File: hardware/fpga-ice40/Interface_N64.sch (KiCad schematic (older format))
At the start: 7 parts, among them J4 Conn_02x20_Odd_Even

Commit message: Reannotate schematic symbols
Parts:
- renumbered J4 to J6, RN7 to RN5, RN5 to RN6, RN8 to RN7, RN6 to RN8
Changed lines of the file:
@@
 P 3500 4300
 AR Path="/5F1CD119" Ref="J?"  Part="1"
-AR Path="/5F133F50/5F1CD119" Ref="J4"  Part="1"
-F 0 "J4" H 3550 5350 50  0000 C CNN
+AR Path="/5F133F50/5F1CD119" Ref="J6"  Part="1"
+F 0 "J6" H 3550 5350 50  0000 C CNN
 F 1 "Conn_02x20_Odd_Even" H 3550 5325 50  0001 C CNN
 F 2 "local_conn:PinHeader_2x20_P2.54mm_Horizontal" H 3500 4300 50  0001 C CNN
@@
 N64_OS_EVENTn
 $Comp
-L ng_power:GND #PWR0126
+L ng_power:GND #PWR026
 U 1 1 5F1CD13A
 P 3900 5400
-F 0 "#PWR0126" H 3900 5150 50  0001 C CNN
+F 0 "#PWR026" H 3900 5150 50  0001 C CNN
 F 1 "GND" H 3903 5274 50  0000 C CNN
 F 2 "" H 3800 5050 50  0001 C CNN
@@
 P 5900 4400
 AR Path="/5F1CD15B" Ref="RN?"  Part="1"
-AR Path="/5F133F50/5F1CD15B" Ref="RN5"  Part="1"
-F 0 "RN5" V 5483 4400 50  0000 C CNN
+AR Path="/5F133F50/5F1CD15B" Ref="RN6"  Part="1"
+F 0 "RN6" V 5483 4400 50  0000 C CNN
 F 1 "33R" V 5574 4400 50  0000 C CNN
 F 2 "Resistor_SMD:R_Array_Convex_4x0603" V 6175 4400 50  0001 C CNN
@@
 P 5900 5100
 AR Path="/5F1CD161" Ref="RN?"  Part="1"
-AR Path="/5F133F50/5F1CD161" Ref="RN6"  Part="1"
-F 0 "RN6" V 5483 5100 50  0000 C CNN
+AR Path="/5F133F50/5F1CD161" Ref="RN8"  Part="1"
+F 0 "RN8" V 5483 5100 50  0000 C CNN
 F 1 "33R" V 5574 5100 50  0000 C CNN
 F 2 "Resistor_SMD:R_Array_Convex_4x0603" V 6175 5100 50  0001 C CNN
@@
 P 7750 3700
 AR Path="/5F1CD167" Ref="RN?"  Part="1"
-AR Path="/5F133F50/5F1CD167" Ref="RN7"  Part="1"
-F 0 "RN7" V 7333 3700 50  0000 C CNN
+AR Path="/5F133F50/5F1CD167" Ref="RN5"  Part="1"
+F 0 "RN5" V 7333 3700 50  0000 C CNN
 F 1 "33R" V 7424 3700 50  0000 C CNN
 F 2 "Resistor_SMD:R_Array_Convex_4x0603" V 8025 3700 50  0001 C CNN
@@
 P 7750 4400
 AR Path="/5F1CD16D" Ref="RN?"  Part="1"
-AR Path="/5F133F50/5F1CD16D" Ref="RN8"  Part="1"
-F 0 "RN8" V 7333 4400 50  0000 C CNN
+AR Path="/5F133F50/5F1CD16D" Ref="RN7"  Part="1"
+F 0 "RN7" V 7333 4400 50  0000 C CNN
 F 1 "33R" V 7424 4400 50  0000 C CNN
 F 2 "Resistor_SMD:R_Array_Convex_4x0603" V 8025 4400 50  0001 C CNN

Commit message: Component selection by MPN and routing cleanup
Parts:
- J6: MPN (none) -> C124369
- RN4, RN5, RN6, RN7, RN8, RN9: value 33R -> 33R, 1%; MPN (none) -> YC164-FR-0733RL
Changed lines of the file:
@@
 F 2 "local_conn:PinHeader_2x20_P2.54mm_Horizontal" H 3500 4300 50  0001 C CNN
 F 3 "~" H 3500 4300 50  0001 C CNN
+F 4 "C124369" H 3500 4300 50  0001 C CNN "MPN"
 	1    3500 4300
 	1    0    0    -1
@@
 AR Path="/5F133F50/5F1CD155" Ref="RN4"  Part="1"
 F 0 "RN4" V 5483 3700 50  0000 C CNN
-F 1 "33R" V 5574 3700 50  0000 C CNN
+F 1 "33R, 1%" V 5574 3700 50  0000 C CNN
 F 2 "Resistor_SMD:R_Array_Convex_4x0603" V 6175 3700 50  0001 C CNN
 F 3 "~" H 5900 3700 50  0001 C CNN
+F 4 "YC164-FR-0733RL" H 5900 3700 50  0001 C CNN "MPN"
 	1    5900 3700
 	0    1    1    0
@@
 AR Path="/5F133F50/5F1CD15B" Ref="RN6"  Part="1"
 F 0 "RN6" V 5483 4400 50  0000 C CNN
-F 1 "33R" V 5574 4400 50  0000 C CNN
+F 1 "33R, 1%" V 5574 4400 50  0000 C CNN
 F 2 "Resistor_SMD:R_Array_Convex_4x0603" V 6175 4400 50  0001 C CNN
 F 3 "~" H 5900 4400 50  0001 C CNN
+F 4 "YC164-FR-0733RL" H 5900 4400 50  0001 C CNN "MPN"
 	1    5900 4400
 	0    1    1    0
@@
 AR Path="/5F133F50/5F1CD161" Ref="RN8"  Part="1"
 F 0 "RN8" V 5483 5100 50  0000 C CNN
-F 1 "33R" V 5574 5100 50  0000 C CNN
+F 1 "33R, 1%" V 5574 5100 50  0000 C CNN
 F 2 "Resistor_SMD:R_Array_Convex_4x0603" V 6175 5100 50  0001 C CNN
 F 3 "~" H 5900 5100 50  0001 C CNN
+F 4 "YC164-FR-0733RL" H 5900 5100 50  0001 C CNN "MPN"
 	1    5900 5100
 	0    1    1    0
@@
 AR Path="/5F133F50/5F1CD167" Ref="RN5"  Part="1"
 F 0 "RN5" V 7333 3700 50  0000 C CNN
-F 1 "33R" V 7424 3700 50  0000 C CNN
+F 1 "33R, 1%" V 7424 3700 50  0000 C CNN
 F 2 "Resistor_SMD:R_Array_Convex_4x0603" V 8025 3700 50  0001 C CNN
 F 3 "~" H 7750 3700 50  0001 C CNN
+F 4 "YC164-FR-0733RL" H 7750 3700 50  0001 C CNN "MPN"
 	1    7750 3700
 	0    1    1    0
@@
 AR Path="/5F133F50/5F1CD16D" Ref="RN7"  Part="1"
 F 0 "RN7" V 7333 4400 50  0000 C CNN
-F 1 "33R" V 7424 4400 50  0000 C CNN
+F 1 "33R, 1%" V 7424 4400 50  0000 C CNN
 F 2 "Resistor_SMD:R_Array_Convex_4x0603" V 8025 4400 50  0001 C CNN
 F 3 "~" H 7750 4400 50  0001 C CNN
+F 4 "YC164-FR-0733RL" H 7750 4400 50  0001 C CNN "MPN"
 	1    7750 4400
 	0    1    1    0
@@
 AR Path="/5F133F50/5F1CD183" Ref="RN9"  Part="1"
 F 0 "RN9" V 7333 5100 50  0000 C CNN
-F 1 "33R" V 7424 5100 50  0000 C CNN
+F 1 "33R, 1%" V 7424 5100 50  0000 C CNN
 F 2 "Resistor_SMD:R_Array_Convex_4x0603" V 8025 5100 50  0001 C CNN
 F 3 "~" H 7750 5100 50  0001 C CNN
+F 4 "YC164-FR-0733RL" H 7750 5100 50  0001 C CNN "MPN"
 	1    7750 5100
 	0    1    1    0

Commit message: Completed verification of all pins for all symbols
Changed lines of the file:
@@
 	3200 4100 3200 4000
 Wire Wire Line
-	3200 4000 3100 4000
-Connection ~ 3200 4000
+	3200 3900 3100 3900
 NoConn ~ 3300 3400
 NoConn ~ 3300 3500
@@
 Text GLabel 4000 5300 2    50   Input ~ 0
 N64_AD15
-Text GLabel 3100 4000 0    50   UnSpc ~ 0
+Text GLabel 3100 3900 0    50   UnSpc ~ 0
 N64_3V3
 $Comp
@@
 Text GLabel 7950 4500 2    50   Input ~ 0
 N64_AD7_IC
+Wire Wire Line
+	3200 3900 3200 4000
+Connection ~ 3200 4000
 $EndSCHEMATC

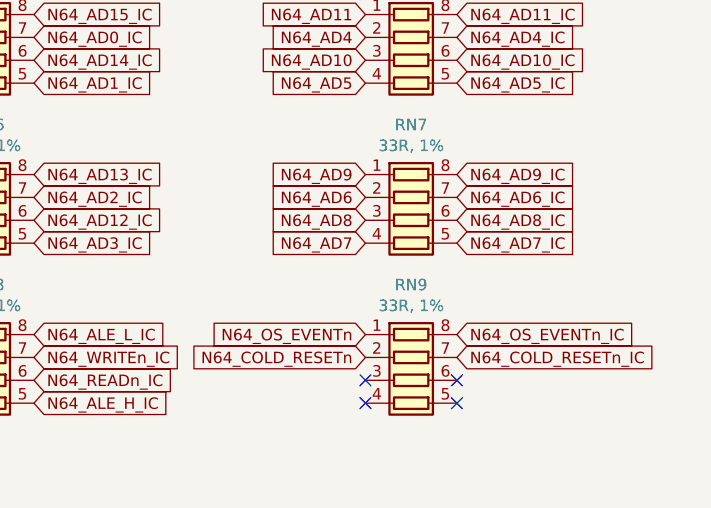
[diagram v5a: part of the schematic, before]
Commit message: Fix mechanical issue by moving USB connector to top of board
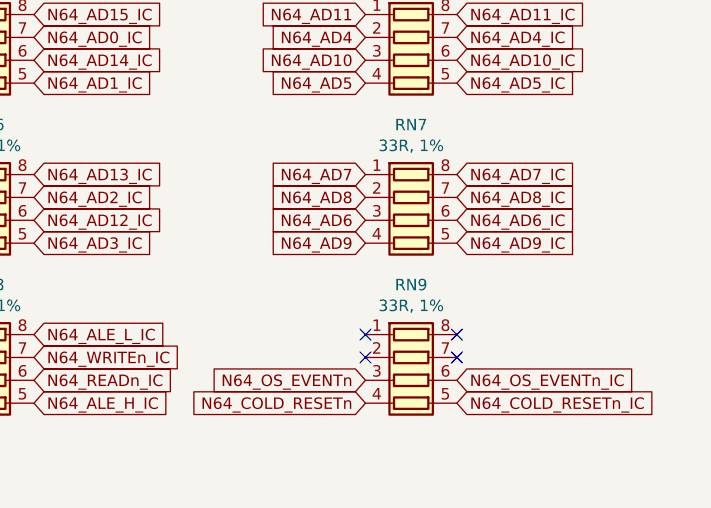
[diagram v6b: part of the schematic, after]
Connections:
- net N64_AD6: now also RN7.3 (R3.1); no longer RN7.2 (R2.1)
- net N64_AD6_IC: now also RN7.6 (R3.2); no longer RN7.7 (R2.2)
- net N64_AD7: now also RN7.1 (R1.1); no longer RN7.4 (R4.1)
- net N64_AD7_IC: now also RN7.8 (R1.2); no longer RN7.5 (R4.2)
- net N64_AD8: now also RN7.2 (R2.1); no longer RN7.3 (R3.1)
- net N64_AD8_IC: now also RN7.7 (R2.2); no longer RN7.6 (R3.2)
- net N64_AD9: now also RN7.4 (R4.1); no longer RN7.1 (R1.1)
- net N64_AD9_IC: now also RN7.5 (R4.2); no longer RN7.8 (R1.2)
- net N64_COLD_RESETn: now also RN9.4 (R4.1); no longer RN9.2 (R2.1)
- net N64_COLD_RESETn_IC: now also RN9.5 (R4.2); no longer RN9.7 (R2.2)
- net N64_OS_EVENTn: now also RN9.3 (R3.1); no longer RN9.1 (R1.1)
- net N64_OS_EVENTn_IC: now also RN9.6 (R3.2); no longer RN9.8 (R1.2)
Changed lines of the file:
@@
 Text GLabel 7550 3700 0    50   Input ~ 0
 N64_AD10
-Text GLabel 7550 4200 0    50   Input ~ 0
+Text GLabel 7550 4500 0    50   Input ~ 0
 N64_AD9
-Text GLabel 7550 4400 0    50   Input ~ 0
+Text GLabel 7550 4300 0    50   Input ~ 0
 N64_AD8
 $Comp
@@
 	0    1    1    0
 $EndComp
-Text GLabel 7550 5000 0    50   Input ~ 0
+Text GLabel 7550 5200 0    50   Input ~ 0
 N64_COLD_RESETn
-Text GLabel 7550 4900 0    50   Input ~ 0
+Text GLabel 7550 5100 0    50   Input ~ 0
 N64_OS_EVENTn
-NoConn ~ 7550 5100
-NoConn ~ 7550 5200
-NoConn ~ 7950 5100
-NoConn ~ 7950 5200
 Text GLabel 7550 3600 0    50   Input ~ 0
 N64_AD4
 Text GLabel 7550 3800 0    50   Input ~ 0
 N64_AD5
-Text GLabel 7550 4300 0    50   Input ~ 0
+Text GLabel 7550 4400 0    50   Input ~ 0
 N64_AD6
-Text GLabel 7550 4500 0    50   Input ~ 0
+Text GLabel 7550 4200 0    50   Input ~ 0
 N64_AD7
 Text GLabel 6100 3600 2    50   Input ~ 0
@@
 Text GLabel 7950 3700 2    50   Input ~ 0
 N64_AD10_IC
-Text GLabel 7950 4200 2    50   Input ~ 0
+Text GLabel 7950 4500 2    50   Input ~ 0
 N64_AD9_IC
-Text GLabel 7950 4400 2    50   Input ~ 0
+Text GLabel 7950 4300 2    50   Input ~ 0
 N64_AD8_IC
-Text GLabel 7950 5000 2    50   Input ~ 0
+Text GLabel 7950 5200 2    50   Input ~ 0
 N64_COLD_RESETn_IC
-Text GLabel 7950 4900 2    50   Input ~ 0
+Text GLabel 7950 5100 2    50   Input ~ 0
 N64_OS_EVENTn_IC
 Text GLabel 7950 3600 2    50   Input ~ 0
@@
 Text GLabel 7950 3800 2    50   Input ~ 0
 N64_AD5_IC
-Text GLabel 7950 4300 2    50   Input ~ 0
+Text GLabel 7950 4400 2    50   Input ~ 0
 N64_AD6_IC
-Text GLabel 7950 4500 2    50   Input ~ 0
+Text GLabel 7950 4200 2    50   Input ~ 0
 N64_AD7_IC
 Wire Wire Line
 	3200 3900 3200 4000
 Connection ~ 3200 4000
+NoConn ~ 7550 4900
+NoConn ~ 7550 5000
+NoConn ~ 7950 4900
+NoConn ~ 7950 5000
 $EndSCHEMATC

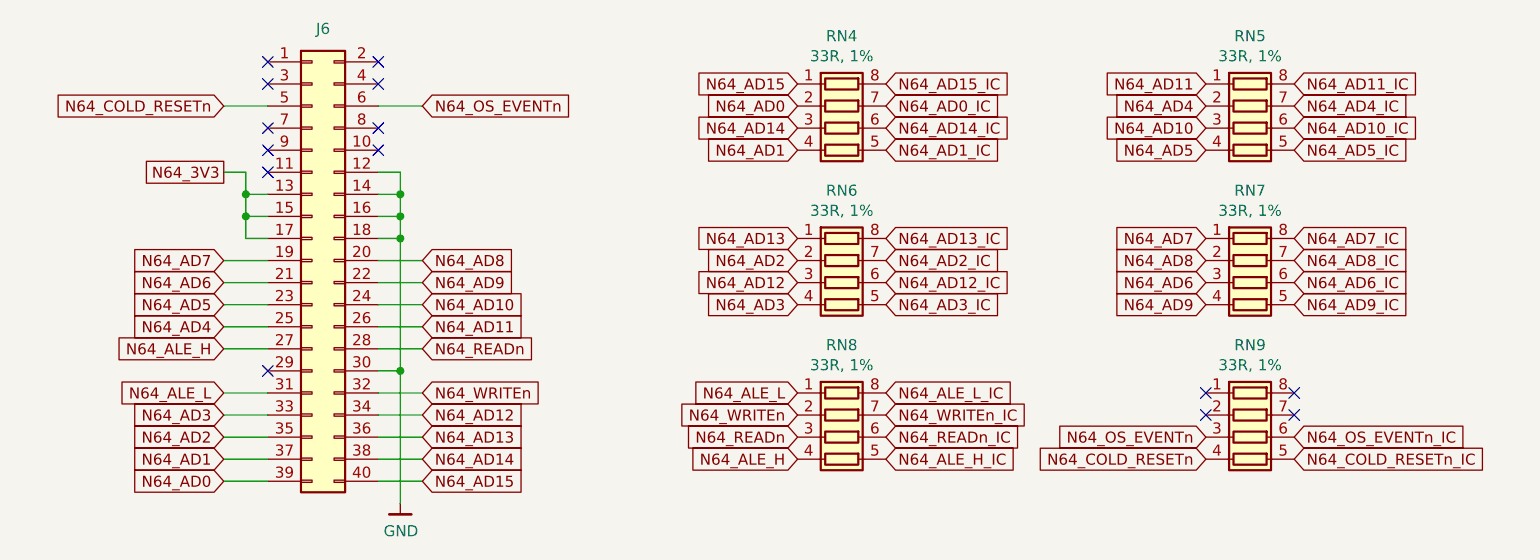
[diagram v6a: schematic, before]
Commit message: Routed N64, DRAM, FIFO, and SD card interfaces
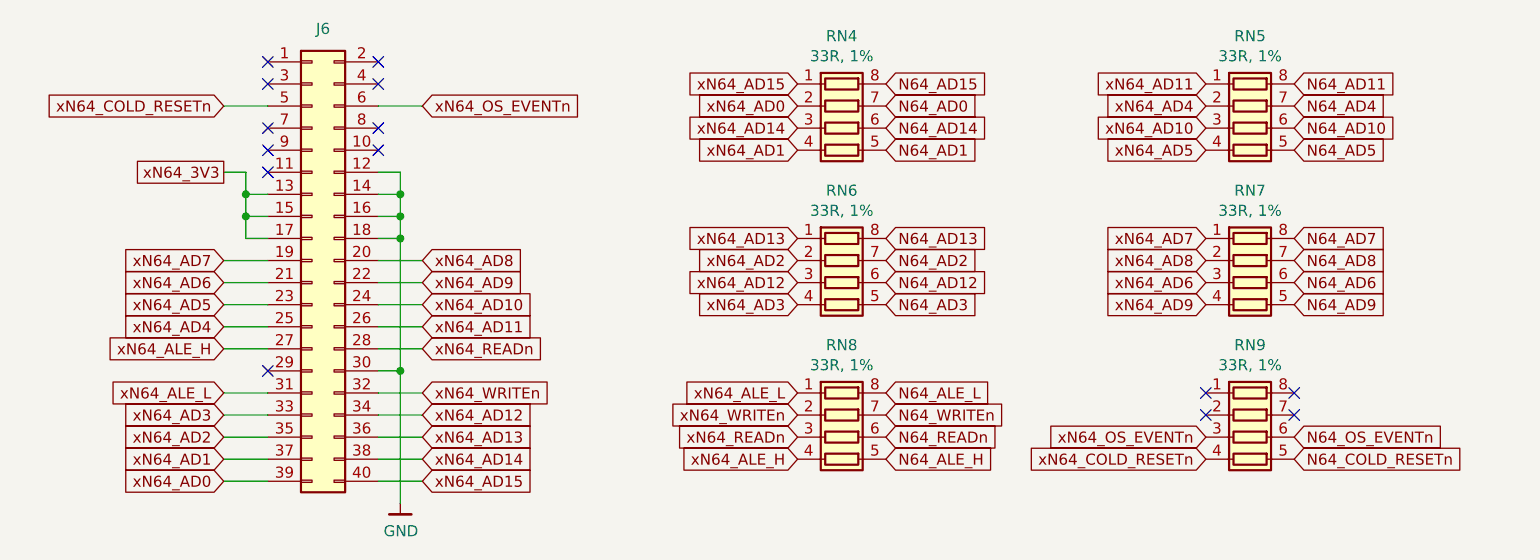
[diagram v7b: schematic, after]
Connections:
- net N64_AD0_IC is gone; now on net N64_AD0: RN4.7 (R2.2)
- net N64_AD10_IC is gone; now on net N64_AD10: RN5.6 (R3.2)
- net N64_AD11_IC is gone; now on net N64_AD11: RN5.8 (R1.2)
- net N64_AD12_IC is gone; now on net N64_AD12: RN6.6 (R3.2)
- net N64_AD13_IC is gone; now on net N64_AD13: RN6.8 (R1.2)
- net N64_AD14_IC is gone; now on net N64_AD14: RN4.6 (R3.2)
- net N64_AD15_IC is gone; now on net N64_AD15: RN4.8 (R1.2)
- net N64_AD1_IC is gone; now on net N64_AD1: RN4.5 (R4.2)
- net N64_AD2_IC is gone; now on net N64_AD2: RN6.7 (R2.2)
- net N64_AD3_IC is gone; now on net N64_AD3: RN6.5 (R4.2)
- net N64_AD4_IC is gone; now on net N64_AD4: RN5.7 (R2.2)
- net N64_AD5_IC is gone; now on net N64_AD5: RN5.5 (R4.2)
- net N64_AD6_IC is gone; now on net N64_AD6: RN7.6 (R3.2)
- net N64_AD7_IC is gone; now on net N64_AD7: RN7.8 (R1.2)
- net N64_AD8_IC is gone; now on net N64_AD8: RN7.7 (R2.2)
- net N64_AD9_IC is gone; now on net N64_AD9: RN7.5 (R4.2)
- net N64_ALE_H_IC is gone; now on net N64_ALE_H: RN8.5 (R4.2)
- net N64_ALE_L_IC is gone; now on net N64_ALE_L: RN8.8 (R1.2)
- net N64_COLD_RESETn_IC is gone; now on net N64_COLD_RESETn: RN9.5 (R4.2)
- net N64_OS_EVENTn_IC is gone; now on net N64_OS_EVENTn: RN9.6 (R3.2)
- net N64_READn_IC is gone; now on net N64_READn: RN8.6 (R3.2)
- net N64_WRITEn_IC is gone; now on net N64_WRITEn: RN8.7 (R2.2)
- net N64_AD0: no longer J6.39 (Pin_39), RN4.2 (R2.1)
- net N64_AD1: no longer J6.37 (Pin_37), RN4.4 (R4.1)
- net N64_AD10: no longer J6.24 (Pin_24), RN5.3 (R3.1)
- net N64_AD11: no longer J6.26 (Pin_26), RN5.1 (R1.1)
- net N64_AD12: no longer J6.34 (Pin_34), RN6.3 (R3.1)
- net N64_AD13: no longer J6.36 (Pin_36), RN6.1 (R1.1)
- net N64_AD14: no longer J6.38 (Pin_38), RN4.3 (R3.1)
- net N64_AD15: no longer J6.40 (Pin_40), RN4.1 (R1.1)
- net N64_AD2: no longer J6.35 (Pin_35), RN6.2 (R2.1)
- net N64_AD3: no longer J6.33 (Pin_33), RN6.4 (R4.1)
- net N64_AD4: no longer J6.25 (Pin_25), RN5.2 (R2.1)
- net N64_AD5: no longer J6.23 (Pin_23), RN5.4 (R4.1)
- net N64_AD6: no longer J6.21 (Pin_21), RN7.3 (R3.1)
- net N64_AD7: no longer J6.19 (Pin_19), RN7.1 (R1.1)
- net N64_AD8: no longer J6.20 (Pin_20), RN7.2 (R2.1)
- net N64_AD9: no longer J6.22 (Pin_22), RN7.4 (R4.1)
- net N64_ALE_H: no longer J6.27 (Pin_27), RN8.4 (R4.1)
- net N64_ALE_L: no longer J6.31 (Pin_31), RN8.1 (R1.1)
- net N64_COLD_RESETn: no longer J6.5 (Pin_5), RN9.4 (R4.1)
- net N64_OS_EVENTn: no longer J6.6 (Pin_6), RN9.3 (R3.1)
- net N64_READn: no longer J6.28 (Pin_28), RN8.3 (R3.1)
- net N64_WRITEn: no longer J6.32 (Pin_32), RN8.2 (R2.1)
- net N64_3V3 renamed xN64_3V3
- new net xN64_AD0: J6.39 (Pin_39), RN4.2 (R2.1)
- new net xN64_AD1: J6.37 (Pin_37), RN4.4 (R4.1)
- new net xN64_AD10: J6.24 (Pin_24), RN5.3 (R3.1)
- new net xN64_AD11: J6.26 (Pin_26), RN5.1 (R1.1)
- new net xN64_AD12: J6.34 (Pin_34), RN6.3 (R3.1)
- new net xN64_AD13: J6.36 (Pin_36), RN6.1 (R1.1)
- new net xN64_AD14: J6.38 (Pin_38), RN4.3 (R3.1)
- new net xN64_AD15: J6.40 (Pin_40), RN4.1 (R1.1)
- new net xN64_AD2: J6.35 (Pin_35), RN6.2 (R2.1)
- new net xN64_AD3: J6.33 (Pin_33), RN6.4 (R4.1)
- new net xN64_AD4: J6.25 (Pin_25), RN5.2 (R2.1)
- new net xN64_AD5: J6.23 (Pin_23), RN5.4 (R4.1)
- new net xN64_AD6: J6.21 (Pin_21), RN7.3 (R3.1)
- new net xN64_AD7: J6.19 (Pin_19), RN7.1 (R1.1)
- new net xN64_AD8: J6.20 (Pin_20), RN7.2 (R2.1)
- new net xN64_AD9: J6.22 (Pin_22), RN7.4 (R4.1)
- new net xN64_ALE_H: J6.27 (Pin_27), RN8.4 (R4.1)
- new net xN64_ALE_L: J6.31 (Pin_31), RN8.1 (R1.1)
- new net xN64_COLD_RESETn: J6.5 (Pin_5), RN9.4 (R4.1)
- new net xN64_OS_EVENTn: J6.6 (Pin_6), RN9.3 (R3.1)
- new net xN64_READn: J6.28 (Pin_28), RN8.3 (R3.1)
- new net xN64_WRITEn: J6.32 (Pin_32), RN8.2 (R2.1)
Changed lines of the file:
@@
 NoConn ~ 3800 3800
 Text GLabel 3100 3600 0    50   Input ~ 0
-N64_COLD_RESETn
+xN64_COLD_RESETn
 Text GLabel 4000 3600 2    50   Input ~ 0
-N64_OS_EVENTn
+xN64_OS_EVENTn
 $Comp
 L ng_power:GND #PWR026
@@
 $EndComp
 Text GLabel 3100 4300 0    50   Input ~ 0
-N64_AD7
+xN64_AD7
 Text GLabel 3100 4400 0    50   Input ~ 0
-N64_AD6
+xN64_AD6
 Text GLabel 3100 4500 0    50   Input ~ 0
-N64_AD5
+xN64_AD5
 Text GLabel 3100 4600 0    50   Input ~ 0
-N64_AD4
+xN64_AD4
 Text GLabel 3100 4700 0    50   Input ~ 0
-N64_ALE_H
+xN64_ALE_H
 Text GLabel 3100 4900 0    50   Input ~ 0
-N64_ALE_L
+xN64_ALE_L
 Text GLabel 3100 5000 0    50   Input ~ 0
-N64_AD3
+xN64_AD3
 Text GLabel 3100 5100 0    50   Input ~ 0
-N64_AD2
+xN64_AD2
 Text GLabel 3100 5200 0    50   Input ~ 0
-N64_AD1
+xN64_AD1
 Text GLabel 3100 5300 0    50   Input ~ 0
-N64_AD0
+xN64_AD0
 Text GLabel 4000 4300 2    50   Input ~ 0
-N64_AD8
+xN64_AD8
 Text GLabel 4000 4400 2    50   Input ~ 0
-N64_AD9
+xN64_AD9
 Text GLabel 4000 4500 2    50   Input ~ 0
-N64_AD10
+xN64_AD10
 Text GLabel 4000 4600 2    50   Input ~ 0
-N64_AD11
+xN64_AD11
 Text GLabel 4000 4700 2    50   Input ~ 0
-N64_READn
+xN64_READn
 Text GLabel 4000 4900 2    50   Input ~ 0
-N64_WRITEn
+xN64_WRITEn
 Text GLabel 4000 5000 2    50   Input ~ 0
-N64_AD12
+xN64_AD12
 Text GLabel 4000 5100 2    50   Input ~ 0
-N64_AD13
+xN64_AD13
 Text GLabel 4000 5200 2    50   Input ~ 0
-N64_AD14
+xN64_AD14
 Text GLabel 4000 5300 2    50   Input ~ 0
-N64_AD15
+xN64_AD15
 Text GLabel 3100 3900 0    50   UnSpc ~ 0
-N64_3V3
+xN64_3V3
 $Comp
 L Device:R_Pack04 RN?
@@
 $EndComp
 Text GLabel 5700 3600 0    50   Input ~ 0
-N64_AD0
+xN64_AD0
 Text GLabel 5700 3500 0    50   Input ~ 0
-N64_AD15
+xN64_AD15
 Text GLabel 5700 3700 0    50   Input ~ 0
-N64_AD14
+xN64_AD14
 Text GLabel 5700 3800 0    50   Input ~ 0
-N64_AD1
+xN64_AD1
 Text GLabel 5700 4300 0    50   Input ~ 0
-N64_AD2
+xN64_AD2
 Text GLabel 5700 4500 0    50   Input ~ 0
-N64_AD3
+xN64_AD3
 Text GLabel 5700 4900 0    50   Input ~ 0
-N64_ALE_L
+xN64_ALE_L
 Text GLabel 5700 5200 0    50   Input ~ 0
-N64_ALE_H
+xN64_ALE_H
 Text GLabel 5700 5000 0    50   Input ~ 0
-N64_WRITEn
+xN64_WRITEn
 Text GLabel 5700 5100 0    50   Input ~ 0
-N64_READn
+xN64_READn
 Text GLabel 5700 4200 0    50   Input ~ 0
-N64_AD13
+xN64_AD13
 Text GLabel 5700 4400 0    50   Input ~ 0
-N64_AD12
+xN64_AD12
 Text GLabel 7550 3500 0    50   Input ~ 0
-N64_AD11
+xN64_AD11
 Text GLabel 7550 3700 0    50   Input ~ 0
-N64_AD10
+xN64_AD10
 Text GLabel 7550 4500 0    50   Input ~ 0
-N64_AD9
+xN64_AD9
 Text GLabel 7550 4300 0    50   Input ~ 0
-N64_AD8
+xN64_AD8
 $Comp
 L Device:R_Pack04 RN?
@@
 $EndComp
 Text GLabel 7550 5200 0    50   Input ~ 0
+xN64_COLD_RESETn
+Text GLabel 7550 5100 0    50   Input ~ 0
+xN64_OS_EVENTn
+Text GLabel 7550 3600 0    50   Input ~ 0
+xN64_AD4
+Text GLabel 7550 3800 0    50   Input ~ 0
+xN64_AD5
+Text GLabel 7550 4400 0    50   Input ~ 0
+xN64_AD6
+Text GLabel 7550 4200 0    50   Input ~ 0
+xN64_AD7
+Text GLabel 6100 3600 2    50   Input ~ 0
+N64_AD0
+Text GLabel 6100 3500 2    50   Input ~ 0
+N64_AD15
+Text GLabel 6100 3700 2    50   Input ~ 0
+N64_AD14
+Text GLabel 6100 3800 2    50   Input ~ 0
+N64_AD1
+Text GLabel 6100 4300 2    50   Input ~ 0
+N64_AD2
+Text GLabel 6100 4500 2    50   Input ~ 0
+N64_AD3
+Text GLabel 6100 4900 2    50   Input ~ 0
+N64_ALE_L
+Text GLabel 6100 5200 2    50   Input ~ 0
+N64_ALE_H
+Text GLabel 6100 5000 2    50   Input ~ 0
+N64_WRITEn
+Text GLabel 6100 5100 2    50   Input ~ 0
+N64_READn
+Text GLabel 6100 4200 2    50   Input ~ 0
+N64_AD13
+Text GLabel 6100 4400 2    50   Input ~ 0
+N64_AD12
+Text GLabel 7950 3500 2    50   Input ~ 0
+N64_AD11
+Text GLabel 7950 3700 2    50   Input ~ 0
+N64_AD10
+Text GLabel 7950 4500 2    50   Input ~ 0
+N64_AD9
+Text GLabel 7950 4300 2    50   Input ~ 0
+N64_AD8
+Text GLabel 7950 5200 2    50   Input ~ 0
 N64_COLD_RESETn
-Text GLabel 7550 5100 0    50   Input ~ 0
+Text GLabel 7950 5100 2    50   Input ~ 0
 N64_OS_EVENTn
-Text GLabel 7550 3600 0    50   Input ~ 0
+Text GLabel 7950 3600 2    50   Input ~ 0
 N64_AD4
-Text GLabel 7550 3800 0    50   Input ~ 0
+Text GLabel 7950 3800 2    50   Input ~ 0
 N64_AD5
-Text GLabel 7550 4400 0    50   Input ~ 0
+Text GLabel 7950 4400 2    50   Input ~ 0
 N64_AD6
-Text GLabel 7550 4200 0    50   Input ~ 0
+Text GLabel 7950 4200 2    50   Input ~ 0
 N64_AD7
-Text GLabel 6100 3600 2    50   Input ~ 0
-N64_AD0_IC
-Text GLabel 6100 3500 2    50   Input ~ 0
-N64_AD15_IC
-Text GLabel 6100 3700 2    50   Input ~ 0
-N64_AD14_IC
-Text GLabel 6100 3800 2    50   Input ~ 0
-N64_AD1_IC
-Text GLabel 6100 4300 2    50   Input ~ 0
-N64_AD2_IC
-Text GLabel 6100 4500 2    50   Input ~ 0
-N64_AD3_IC
-Text GLabel 6100 4900 2    50   Input ~ 0
-N64_ALE_L_IC
-Text GLabel 6100 5200 2    50   Input ~ 0
-N64_ALE_H_IC
-Text GLabel 6100 5000 2    50   Input ~ 0
-N64_WRITEn_IC
-Text GLabel 6100 5100 2    50   Input ~ 0
-N64_READn_IC
-Text GLabel 6100 4200 2    50   Input ~ 0
-N64_AD13_IC
-Text GLabel 6100 4400 2    50   Input ~ 0
-N64_AD12_IC
-Text GLabel 7950 3500 2    50   Input ~ 0
-N64_AD11_IC
-Text GLabel 7950 3700 2    50   Input ~ 0
-N64_AD10_IC
-Text GLabel 7950 4500 2    50   Input ~ 0
-N64_AD9_IC
-Text GLabel 7950 4300 2    50   Input ~ 0
-N64_AD8_IC
-Text GLabel 7950 5200 2    50   Input ~ 0
-N64_COLD_RESETn_IC
-Text GLabel 7950 5100 2    50   Input ~ 0
-N64_OS_EVENTn_IC
-Text GLabel 7950 3600 2    50   Input ~ 0
-N64_AD4_IC
-Text GLabel 7950 3800 2    50   Input ~ 0
-N64_AD5_IC
-Text GLabel 7950 4400 2    50   Input ~ 0
-N64_AD6_IC
-Text GLabel 7950 4200 2    50   Input ~ 0
-N64_AD7_IC
 Wire Wire Line
 	3200 3900 3200 4000
